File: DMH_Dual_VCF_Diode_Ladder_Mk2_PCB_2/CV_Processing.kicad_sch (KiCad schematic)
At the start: 50 parts, among them J15 Conn_01x08_PinHeader, J16 Conn_01x08_PinHeader, SW10 SW_DPDT_OnOn, SW7 SW_SPDT_OnOffOn, SW9 SW_SPDT_OnOffOn, U7 TL074, U8 TL074

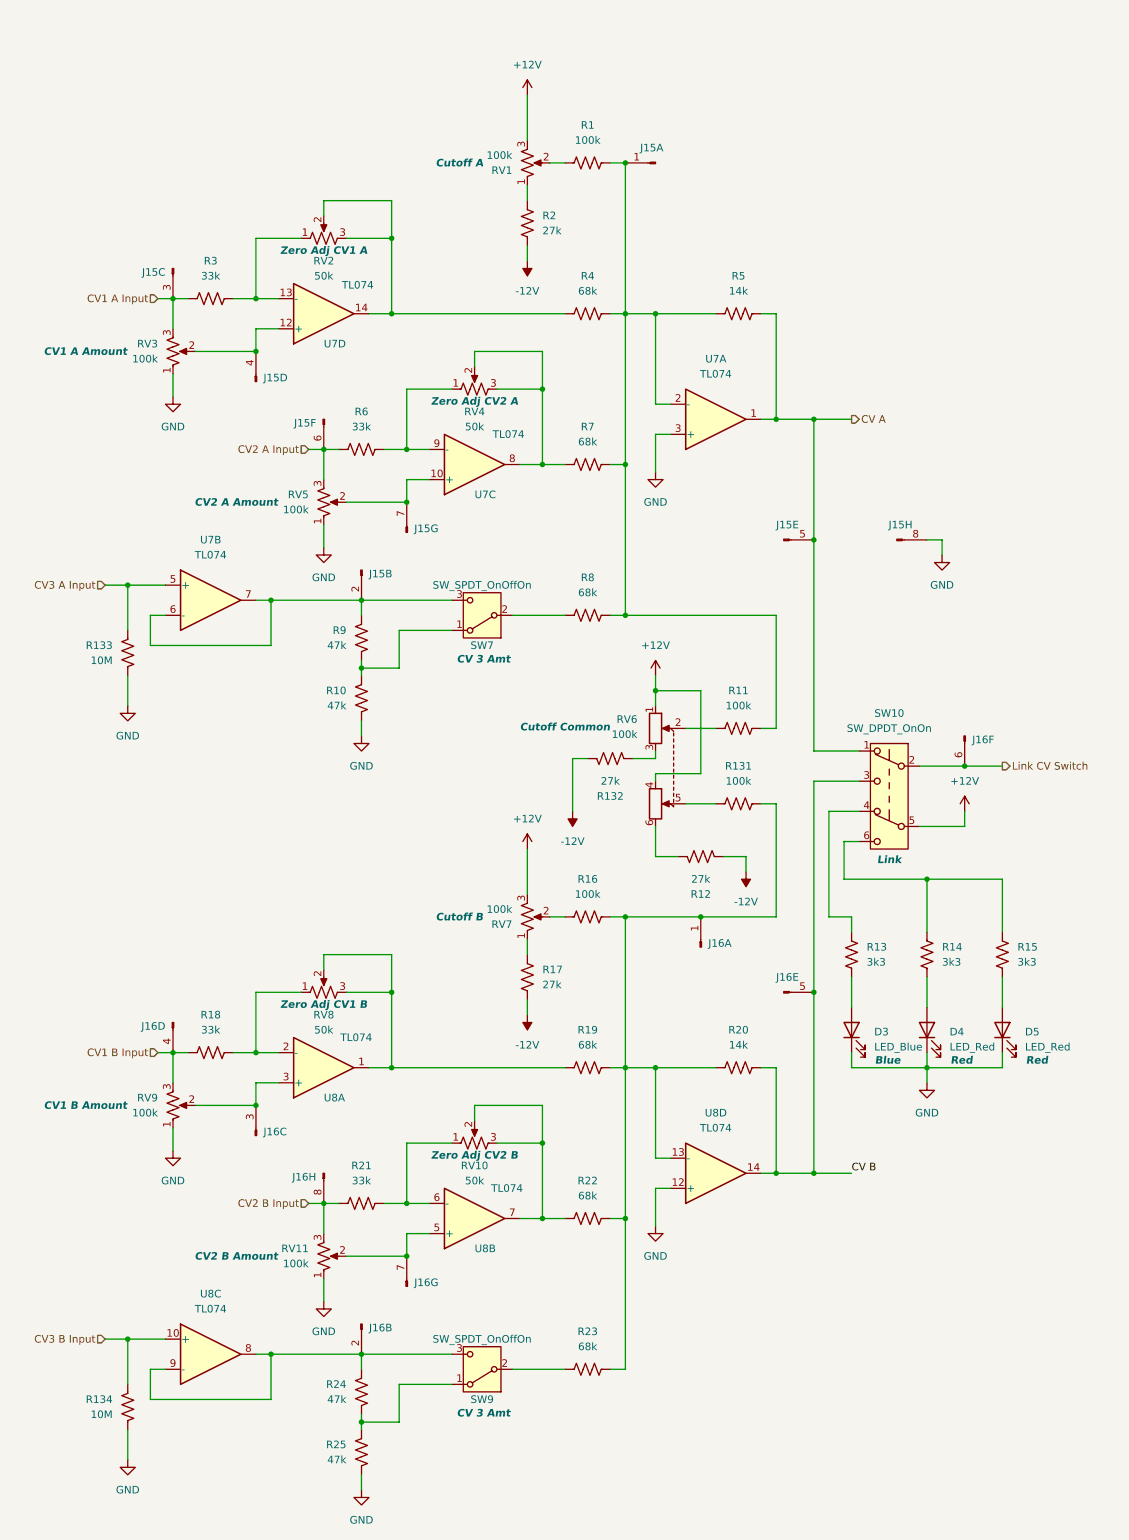
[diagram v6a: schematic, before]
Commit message: Synchronized changes from PCB 1 to PCB 2 schematic
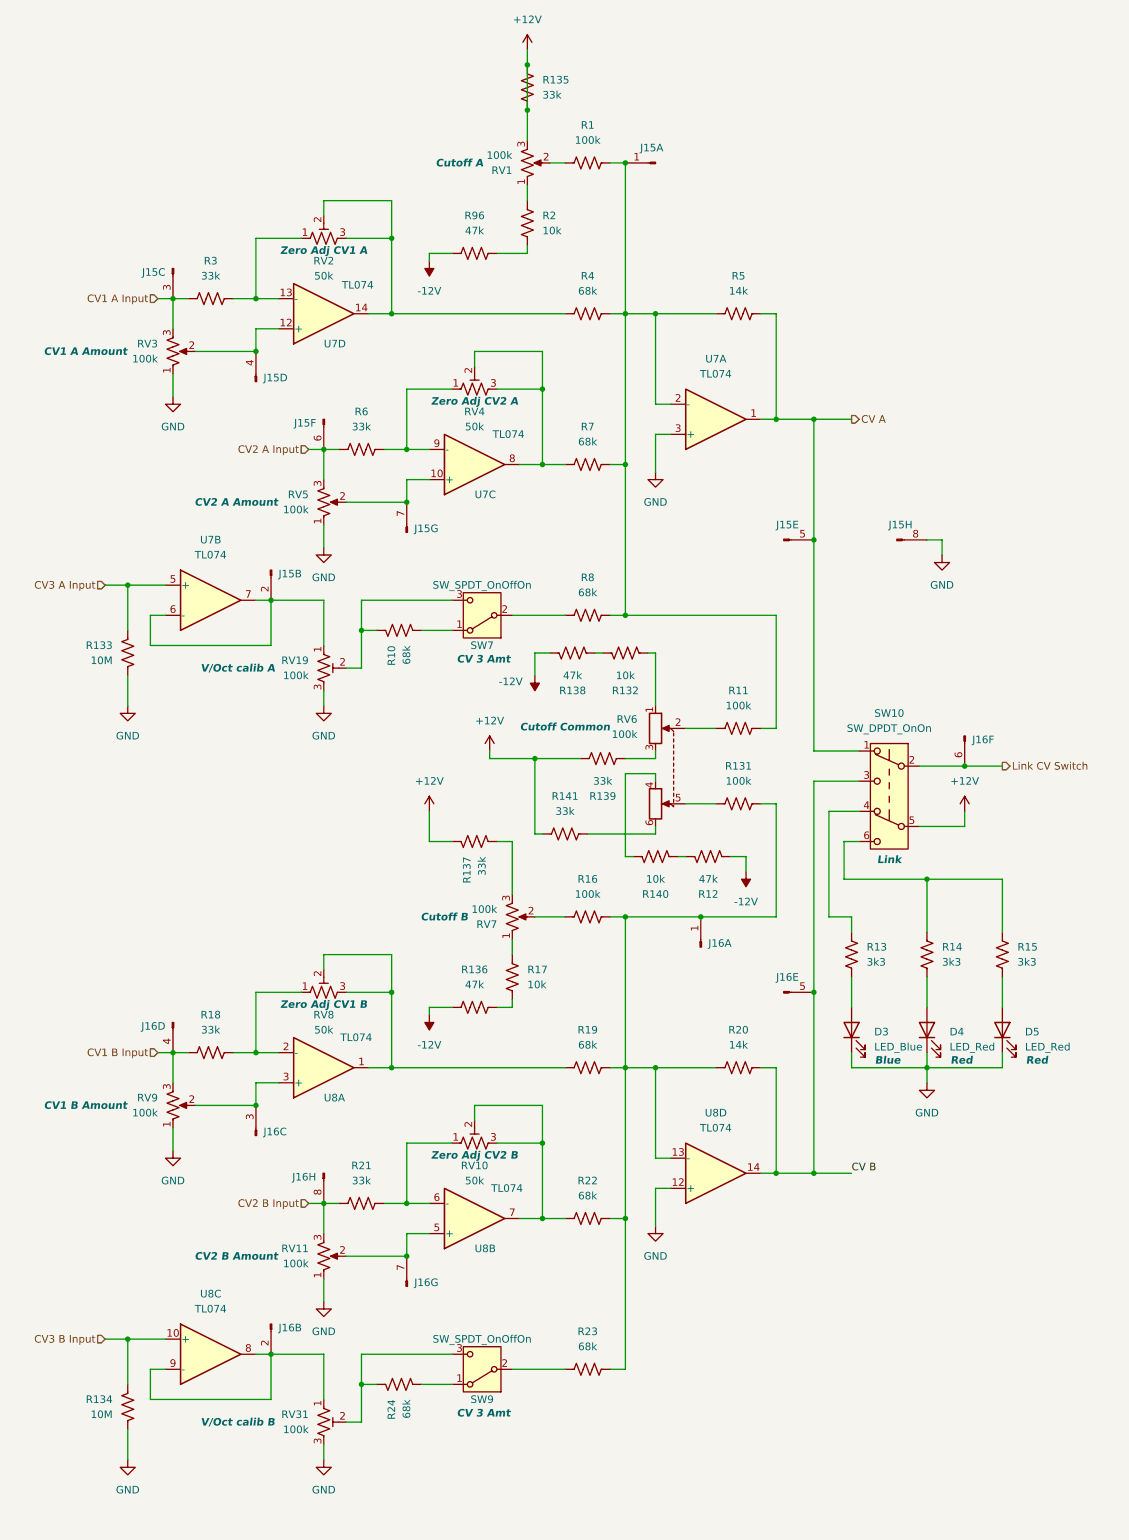
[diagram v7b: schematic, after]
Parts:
- removed R25, R9: 47k, Resistor_THT:R_Axial_DIN0207_L6.3mm_D2.5mm_P7.62mm_Horizontal, symbol Device:R_US
- added R135, R137, R139, R141: 33k, Resistor_THT:R_Axial_DIN0207_L6.3mm_D2.5mm_P7.62mm_Horizontal, symbol Device:R_US
- added R136, R138, R96: 47k, Resistor_THT:R_Axial_DIN0207_L6.3mm_D2.5mm_P7.62mm_Horizontal, symbol Device:R_US
- added R140: 10k, Resistor_THT:R_Axial_DIN0207_L6.3mm_D2.5mm_P7.62mm_Horizontal, symbol Device:R_US
- added RV19, RV31: 100k, symbol Device:R_Potentiometer_Trim_US
- R10, R24: value 47k -> 68k
- R12: value 27k -> 47k
- R132, R17, R2: value 27k -> 10k
- RV10, RV2, RV4, RV8: symbol Device:R_Potentiometer_US -> Device:R_Potentiometer_Trim_US
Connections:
- net +12V: now also R135.1, R135.2, R137.1, R139.2, R141.1; no longer RV6.1, RV6.4, RV7.3
- net -12V: now also R136.1, R138.2, R96.1; no longer R132.2, R17.2, R2.2
- net GND: now also RV19.3, RV31.3; no longer R10.1
- net at J15.2 (Pin_2), U7.6 (-), U7.7: now also RV19.1; no longer SW7.3 (C)
- net at SW7.1 (A): now also R10.1; no longer R10.2
- net at RV6.3: now also R139.1; no longer R132.1
- net at J16.2 (Pin_2), U8.8, U8.9 (-): now also RV31.1; no longer R24.2, SW9.3 (C)
- net at RV6.6: now also R141.2; no longer R12.1
- new net: R136.2, R17.2
- new net: R2.2, R96.2
- new net: R24.2, RV31.2, SW9.3 (C)
- new net: R10.2, RV19.2, SW7.3 (C)
- new net: R132.1, RV6.1
- new net: R132.2, R138.1
- new net: R137.2, RV7.3
- new net: R140.1, RV6.4
- new net: R12.1, R140.2
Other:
- moved on the sheet: J15B, J16B, R10, R12, R132, R17, R24, RV7

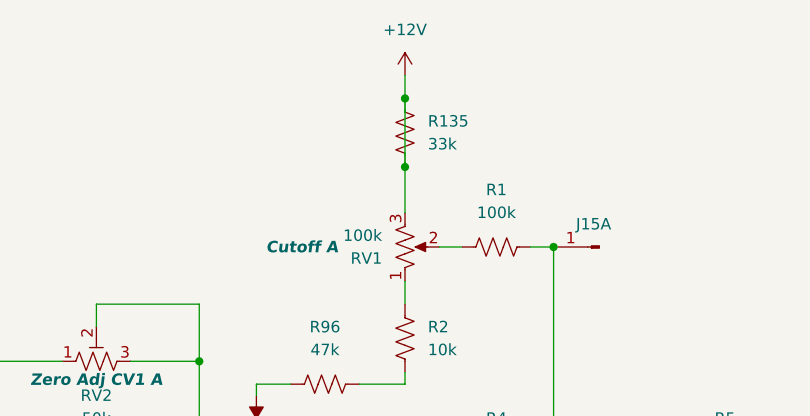
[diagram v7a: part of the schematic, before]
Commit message: Updated PCB 2 with validated features
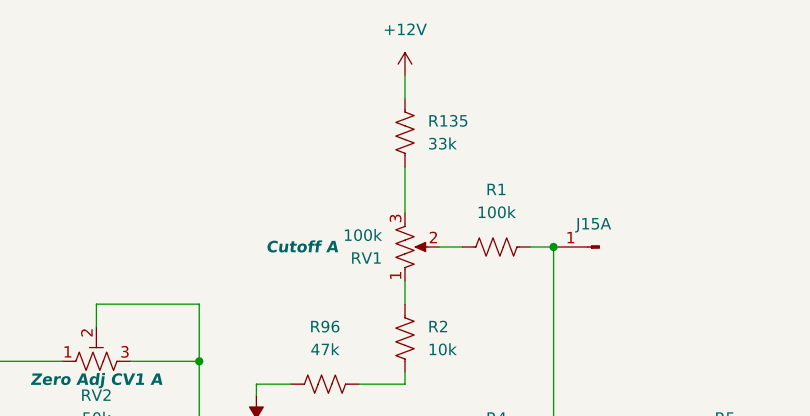
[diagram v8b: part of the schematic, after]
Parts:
- RV19, RV31: footprint (none) -> Potentiometer_THT:Potentiometer_Bourns_3296W_Vertical
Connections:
- net +12V: no longer R135.1, RV1.3
- new net: R135.1, RV1.3
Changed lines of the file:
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@@
 	)
 	(junction
-		(at 97.79 21.59)
-		(diameter 0)
-		(color 0 0 0 0)
-	)
-	(junction
 		(at 114.3 114.3)
 		(diameter 0)
@@
 	)
 	(junction
-		(at 97.79 29.21)
-		(diameter 0)
-		(color 0 0 0 0)
-	)
-	(junction
 		(at 165.1 158.75)
 		(diameter 0)
@@
 	(wire
 		(pts
-			(xy 97.79 21.59) (xy 97.79 29.21)
-		)
-		(stroke
-			(width 0)
-			(type default)
-		)
-	)
-	(wire
-		(pts
 			(xy 30.48 236.22) (xy 30.48 243.84)
 		)
@@
 			)
 		)
-		(property "Footprint" ""
+		(property "Footprint" "Potentiometer_THT:Potentiometer_Bourns_3296W_Vertical"
 			(at 63.5 250.19 0)
 			(effects
@@
 		(exclude_from_sim no)
 		(in_bom yes)
-		(on_board yes)
+		(on_board no)
 		(dnp no)
 		(property "Reference" "RV10"
@@
 		(exclude_from_sim no)
 		(in_bom yes)
-		(on_board yes)
+		(on_board no)
 		(dnp no)
 		(property "Reference" "RV8"
@@
 		(exclude_from_sim no)
 		(in_bom yes)
-		(on_board yes)
+		(on_board no)
 		(dnp no)
 		(property "Reference" "RV4"
@@
 		(exclude_from_sim no)
 		(in_bom yes)
-		(on_board yes)
+		(on_board no)
 		(dnp no)
 		(property "Reference" "RV2"
@@
 			)
 		)
-		(property "Footprint" ""
+		(property "Footprint" "Potentiometer_THT:Potentiometer_Bourns_3296W_Vertical"
 			(at 63.5 123.19 0)
 			(effects
